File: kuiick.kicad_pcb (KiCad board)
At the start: 2 copper layers, 15 x 19 mm, 22 parts, among them J1 10118193-0001LF, J2 I2C_STANDARDQWIIC, J3 Conn_01x07, J4 Conn_01x07, SW1 SW_SPST, SW2 SW_SPST, U1 MK32L2B_QFN32, U2 W25Q32JVSS

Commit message: fully routed dip 16
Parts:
- J3, J4: value Conn_01x07 -> Conn_01x08; footprint footprint:PinHeader_1x07_P100mil_Vertical -> footprint:PinHeader_1x08_P100mil_Vertical
- moved R7 1.80 mm to (146.0, 97.8)
- moved J3 1.27 mm to (143.7, 108.9)
- moved J4 1.27 mm to (156.3, 108.9)
- moved R5 1.04 mm to (145.7, 93.0), turned to 90 degrees
- moved C1 0.82 mm to (149.8, 105.1), turned to 0 degrees
- moved J1 0.50 mm to (150.0, 108.6)
- moved J2 0.40 mm to (150.0, 94.8)
- moved U2 0.40 mm to (150.0, 93.0)
- moved R4 0.30 mm to (145.7, 95.0), turned to -90 degrees
- moved C8 0.30 mm to (154.0, 94.0)
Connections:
- J3 pad 1: /AN -> /NMI#
- J3 pad 2: /NMI# -> /RST#
- J3 pad 3: /RST# -> /SWC
- J3 pad 4: /SWC -> /SWD
- J3 pad 5: /SWD -> GND
- J3 pad 6: GND -> /3V3
- J3 pad 7: /3V3 -> /SCL
- J4 pad 1: /+5V -> /AN
- J4 pad 2: /FX7 -> /+5V
- J4 pad 3: /FX6 -> /FX7
- J4 pad 4: /FX5 -> /FX6
- J4 pad 5: /FX4 -> /FX5
- J4 pad 6: GND -> /FX4
- J4 pad 7: /3V3 -> GND
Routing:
- net GND: track 80.8 -> 66.5 mm, vias 13 -> 14
- net /AN: track 8.68 -> 17.6 mm
- net /3V3: track 61.3 -> 56.6 mm
- net /SDA: track 6.51 -> 11.0 mm
- net /RST#: track 14.9 -> 19.4 mm
- net /SCL: track 5.28 -> 8.89 mm
- net /G: track 10.4 -> 13.6 mm
- net /NMI#: track 12.2 -> 15.0 mm
- net /SWC: track 4.43 -> 5.65 mm
- net /SWD: track 5.21 -> 4.32 mm
- net /MOSI: track 16.9 -> 17.7 mm
- net /FX4: track 5.30 -> 5.92 mm
- net /FX6: track 4.45 -> 3.92 mm
- net /FX7: track 5.29 -> 4.77 mm
- net /FX5: track 4.22 -> 4.75 mm
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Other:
- board size 15 x 19 mm -> 15 x 20 mm

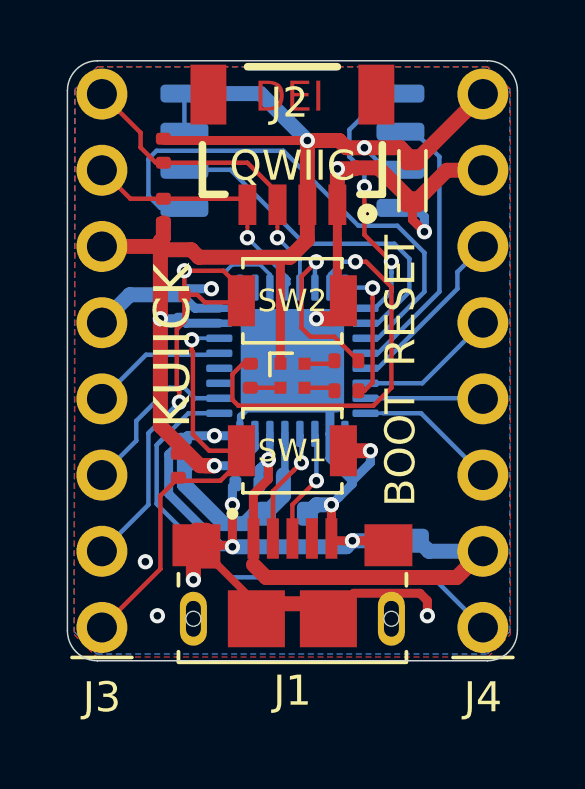
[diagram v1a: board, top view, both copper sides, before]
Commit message: cleaned up silk, added logo
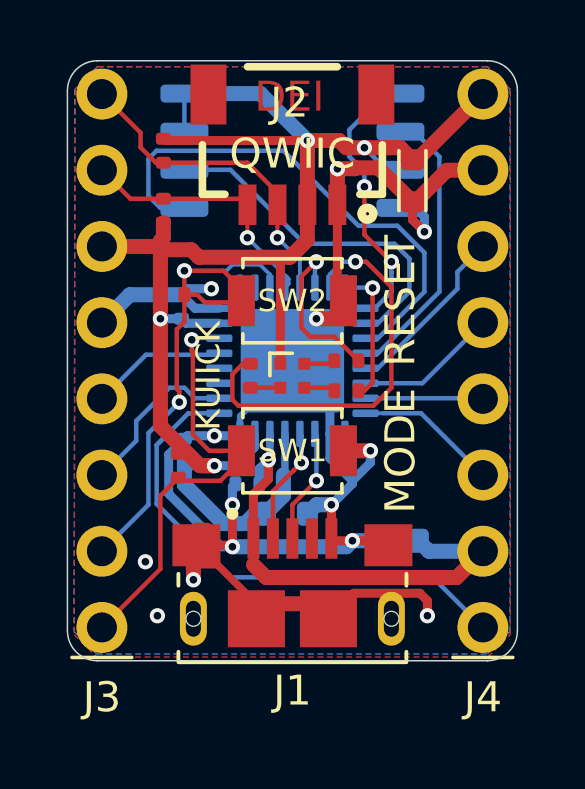
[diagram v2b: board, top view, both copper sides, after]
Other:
- board text added: "+3"
- board text added: "+5"
- board text added: "GND"
- board text added: "MODE"
- board text added: "SCL"
- board text added: "SDA"
- board text removed: "3V"
- board text removed: "5V"
- board text removed: "BOOT"
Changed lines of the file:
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@@
   (general
     (thickness 1.6)
-    (drawings 31)
+    (drawings 35)
     (tracks 356)
     (modules 22)
@@
   (layers
     (0 "F.Cu" signal)
-    (31 "B.Cu" signal)
-    (32 "B.Adhes" user)
-    (33 "F.Adhes" user)
-    (34 "B.Paste" user)
+    (31 "B.Cu" signal hide)
+    (32 "B.Adhes" user hide)
+    (33 "F.Adhes" user hide)
+    (34 "B.Paste" user hide)
     (35 "F.Paste" user)
-    (36 "B.SilkS" user)
+    (36 "B.SilkS" user hide)
     (37 "F.SilkS" user)
-    (38 "B.Mask" user)
+    (38 "B.Mask" user hide)
     (39 "F.Mask" user)
-    (40 "Dwgs.User" user)
-    (41 "Cmts.User" user)
-    (42 "Eco1.User" user)
-    (43 "Eco2.User" user)
+    (40 "Dwgs.User" user hide)
+    (41 "Cmts.User" user hide)
+    (42 "Eco1.User" user hide)
+    (43 "Eco2.User" user hide)
     (44 "Edge.Cuts" user)
-    (45 "Margin" user)
-    (46 "B.CrtYd" user)
+    (45 "Margin" user hide)
+    (46 "B.CrtYd" user hide)
     (47 "F.CrtYd" user)
-    (48 "B.Fab" user)
+    (48 "B.Fab" user hide)
     (49 "F.Fab" user)
   )
@@
       (net 1 "GND") (solder_mask_margin 0.1016))
   )
+  (gr_poly (pts (xy 153.5 103.183334) (xy 154.029167 104.241667) (xy 152.970834 104.241667) (xy 153.5 105.3) (xy 152.441667 104.241667) (xy 152.812084 103.87125) (xy 153.5 103.87125) (xy 153.5 103.765417) (xy 152.917917 103.765417) (xy 153.5 103.183334)) (layer "B.SilkS") (width 0.010583))
+  (gr_poly (pts (xy 153.5 103.183334) (xy 154.558333 104.241667) (xy 153.5 105.3) (xy 152.970834 104.241667) (xy 153.881 104.241667) (xy 153.5 104.622667) (xy 153.5 104.770833) (xy 154.029167 104.241667) (xy 153.5 103.183334)) (layer "B.Mask") (width 0.010583))
+  (gr_text "SCL" (at 145 93.8 270) (layer "B.SilkS")
+    (effects (font (size 0.75 0.75) (thickness 0.15)) (justify mirror))
+  )
+  (gr_text "SDA" (at 145 91.3 270) (layer "B.SilkS")
+    (effects (font (size 0.75 0.75) (thickness 0.15)) (justify mirror))
+  )
   (gr_text "DEI" (at 149.9 91.2) (layer "F.Cu")
     (effects (font (size 1 1) (thickness 0.15)))
   )
-  (gr_text "Steiert\nSolutions" (at 150 108.2) (layer "B.SilkS")
-    (effects (font (size 0.75 0.75) (thickness 0.15)) (justify mirror))
-  )
-  (gr_text "by" (at 151.3 105.8) (layer "B.SilkS")
-    (effects (font (size 0.75 0.75) (thickness 0.15)) (justify mirror))
-  )
-  (gr_text "KUIICK" (at 151.4 103.9) (layer "B.SilkS")
-    (effects (font (size 0.75 0.75) (thickness 0.15)) (justify mirror))
-  )
-  (gr_text "QWIIC" (at 150 93.5) (layer "F.SilkS")
+  (gr_text "Steiert\nSolutions" (at 150 108.7) (layer "B.SilkS")
+    (effects (font (size 0.75 0.75) (thickness 0.15)) (justify mirror))
+  )
+  (gr_text "by" (at 150 112) (layer "B.SilkS")
+    (effects (font (size 0.75 0.75) (thickness 0.15)) (justify mirror))
+  )
+  (gr_text "KUIICK" (at 149.9 106.5) (layer "B.SilkS")
+    (effects (font (size 0.75 0.75) (thickness 0.15)) (justify mirror))
+  )
+  (gr_text "QWIIC" (at 150 93.1) (layer "F.SilkS")
     (effects (font (size 1 1) (thickness 0.15)))
   )
-  (gr_text "KUIICK" (at 146 99.5 90) (layer "F.SilkS")
-    (effects (font (size 1.2 1.2) (thickness 0.2)))
-  )
-  (gr_text "BOOT" (at 153.6 102.9 90) (layer "F.SilkS")
+  (gr_text "KUIICK" (at 147.2 100.5 90) (layer "F.SilkS")
+    (effects (font (size 0.8 0.8) (thickness 0.2)))
+  )
+  (gr_text "MODE" (at 153.6 103 90) (layer "F.SilkS")
     (effects (font (size 1 1) (thickness 0.15)))
   )
@@
     (effects (font (size 0.75 0.75) (thickness 0.15)) (justify mirror))
   )
-  (gr_text "3V" (at 155.2 91.2) (layer "B.SilkS")
-    (effects (font (size 0.75 0.75) (thickness 0.15)) (justify mirror))
-  )
-  (gr_text "G" (at 155.2 93.9) (layer "B.SilkS")
-    (effects (font (size 0.75 0.75) (thickness 0.15)) (justify mirror))
-  )
-  (gr_text "G" (at 144.7 93.7) (layer "B.SilkS")
-    (effects (font (size 0.75 0.75) (thickness 0.15)) (justify mirror))
-  )
-  (gr_text "3V" (at 144.8 91.2) (layer "B.SilkS")
-    (effects (font (size 0.75 0.75) (thickness 0.15)) (justify mirror))
-  )
-  (gr_text "F7" (at 154.6 104.7) (layer "B.SilkS")
-    (effects (font (size 0.75 0.75) (thickness 0.15)) (justify mirror))
-  )
-  (gr_text "F6" (at 154.6 102.5) (layer "B.SilkS")
-    (effects (font (size 0.75 0.75) (thickness 0.15)) (justify mirror))
-  )
-  (gr_text "F5" (at 154.6 100.1) (layer "B.SilkS")
-    (effects (font (size 0.75 0.75) (thickness 0.15)) (justify mirror))
-  )
-  (gr_text "F4" (at 154.6 97.5) (layer "B.SilkS")
-    (effects (font (size 0.75 0.75) (thickness 0.15)) (justify mirror))
-  )
-  (gr_text "5V" (at 154.6 107.6) (layer "B.SilkS")
-    (effects (font (size 0.75 0.75) (thickness 0.15)) (justify mirror))
-  )
-  (gr_text "AN" (at 145.3 107.7) (layer "B.SilkS")
-    (effects (font (size 0.75 0.75) (thickness 0.15)) (justify mirror))
-  )
-  (gr_text "NMI" (at 145.7 105.1) (layer "B.SilkS")
-    (effects (font (size 0.75 0.75) (thickness 0.15)) (justify mirror))
-  )
-  (gr_text "RST" (at 145.6 101.8) (layer "B.SilkS")
-    (effects (font (size 0.75 0.75) (thickness 0.15)) (justify mirror))
-  )
-  (gr_text "SWC" (at 145.9 96.9) (layer "B.SilkS")
-    (effects (font (size 0.75 0.75) (thickness 0.15)) (justify mirror))
-  )
-  (gr_text "SWD" (at 145.8 100) (layer "B.SilkS")
-    (effects (font (size 0.75 0.75) (thickness 0.15)) (justify mirror))
-  )
+  (gr_text "+3" (at 155.4 92.3) (layer "B.SilkS")
+    (effects (font (size 0.75 0.75) (thickness 0.15)) (justify mirror))
+  )
+  (gr_text "G" (at 155.2 94.6) (layer "B.SilkS")
+    (effects (font (size 0.75 0.75) (thickness 0.15)) (justify mirror))
+  )
+  (gr_text "GND" (at 145.2 98.7 270) (layer "B.SilkS")
+    (effects (font (size 0.75 0.75) (thickness 0.15)) (justify mirror))
+  )
+  (gr_text "+3" (at 145.2 96.4 270) (layer "B.SilkS")
+    (effects (font (size 0.75 0.75) (thickness 0.15)) (justify mirror))
+  )
+  (gr_text "F7" (at 154.6 102.7) (layer "B.SilkS")
+    (effects (font (size 0.75 0.75) (thickness 0.15)) (justify mirror))
+  )
+  (gr_text "F6" (at 154.6 101.3) (layer "B.SilkS")
+    (effects (font (size 0.75 0.75) (thickness 0.15)) (justify mirror))
+  )
+  (gr_text "F5" (at 154.6 98.8) (layer "B.SilkS")
+    (effects (font (size 0.75 0.75) (thickness 0.15)) (justify mirror))
+  )
+  (gr_text "F4" (at 154.6 96.7) (layer "B.SilkS")
+    (effects (font (size 0.75 0.75) (thickness 0.15)) (justify mirror))
+  )
+  (gr_text "+5" (at 155.1 107.2) (layer "B.SilkS")
+    (effects (font (size 0.75 0.75) (thickness 0.15)) (justify mirror))
+  )
+  (gr_text "AN" (at 154.7 109.3) (layer "B.SilkS")
+    (effects (font (size 0.75 0.75) (thickness 0.15)) (justify mirror))
+  )
+  (gr_text "NMI" (at 145.2 108.8 270) (layer "B.SilkS")
+    (effects (font (size 0.75 0.75) (thickness 0.15)) (justify mirror))
+  )
+  (gr_text "RST" (at 145.2 106.4 270) (layer "B.SilkS")
+    (effects (font (size 0.75 0.75) (thickness 0.15)) (justify mirror))
+  )
+  (gr_text "SWC" (at 145.2 103.8 270) (layer "B.SilkS")
+    (effects (font (size 0.75 0.75) (thickness 0.15)) (justify mirror))
+  )
+  (gr_text "SWD" (at 145.2 101.3 270) (layer "B.SilkS")
+    (effects (font (size 0.75 0.75) (thickness 0.15)) (justify mirror))
+  )

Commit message: clean up silk, swapped qwiic footprint
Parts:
- J2: footprint Connectors:1X04_1MM_RA -> Connector_JST:JST_SH_SM04B-SRSS-TB_1x04-1MP_P1.00mm_Horizontal
- moved J2 2.00 mm to (150.0, 92.8)
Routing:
- net /RST#: track 19.4 -> 17.4 mm
- net /SCL: track 8.89 -> 8.31 mm
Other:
- board text added: "K32L USB to IIC Kit"
- board text removed: "by"

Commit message: clean up fills
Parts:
- moved C8 0.41 mm to (154.1, 93.6)
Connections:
- J1 pad None: (no net) -> GND
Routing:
- net GND: track 66.5 -> 75.7 mm, vias 14 -> 15
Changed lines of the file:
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@@
     (thickness 1.6)
     (drawings 37)
-    (tracks 351)
+    (tracks 357)
     (modules 22)
     (nets 33)
@@
       (dielectric_constraints no)
     )
-    (last_trace_width 0.3)
+    (last_trace_width 0.25)
     (user_trace_width 0.127)
     (user_trace_width 0.15)
@@
     (pad "S5" thru_hole oval (at -3.3 0) (size 0.9 1.8) (drill oval 0.5 1.2) (layers *.Cu *.Mask)
       (net 1 "GND"))
-    (pad "None" np_thru_hole circle (at 3.3 0) (size 0.5 0.5) (drill 0.5) (layers *.Cu *.Mask))
+    (pad "None" np_thru_hole circle (at 3.3 0) (size 0.5 0.5) (drill 0.5) (layers *.Cu *.Mask)
+      (net 1 "GND"))
     (pad "None" np_thru_hole circle (at -3.3 0) (size 0.5 0.5) (drill 0.5) (layers *.Cu *.Mask))
     (pad "S3" smd rect (at 1.2 0) (size 1.9 1.9) (layers "F.Cu" "F.Paste" "F.Mask")
@@
   )
   (module "footprint:C0603" (layer "F.Cu")
-    (at 154 94 -90)
+    (at 154.1 93.6 -90)
     (descr "Capacitor SMD 0603 (1608 Metric), square (rectangular) end terminal, IPC_7351 nominal, (Body size source: http://www.tortai-tech.com/upload/download/2011102023233369053.pdf), generated with kicad-footprint-generator")
     (tags "capacitor")
@@
   )
   (dimension 20 (width 0.1) (layer "Dwgs.User")
-    (gr_text "20.000 mm" (at 162.25 100 270) (layer "Dwgs.User")
-      (effects (font (size 1 1) (thickness 0.15)))
-    )
-    (feature1 (pts (xy 160 110) (xy 161.586421 110)))
-    (feature2 (pts (xy 160 90) (xy 161.586421 90)))
-    (crossbar (pts (xy 161 90) (xy 161 110)))
-    (arrow1a (pts (xy 161 110) (xy 160.413579 108.873496)))
-    (arrow1b (pts (xy 161 110) (xy 161.586421 108.873496)))
-    (arrow2a (pts (xy 161 90) (xy 160.413579 91.126504)))
-    (arrow2b (pts (xy 161 90) (xy 161.586421 91.126504)))
+    (gr_text "20.000 mm" (at 161.75 100 270) (layer "Dwgs.User")
+      (effects (font (size 1 1) (thickness 0.15)))
+    )
+    (feature1 (pts (xy 159.5 110) (xy 161.086421 110)))
+    (feature2 (pts (xy 159.5 90) (xy 161.086421 90)))
+    (crossbar (pts (xy 160.5 90) (xy 160.5 110)))
+    (arrow1a (pts (xy 160.5 110) (xy 159.913579 108.873496)))
+    (arrow1b (pts (xy 160.5 110) (xy 161.086421 108.873496)))
+    (arrow2a (pts (xy 160.5 90) (xy 159.913579 91.126504)))
+    (arrow2b (pts (xy 160.5 90) (xy 161.086421 91.126504)))
   )
   (gr_text "KUIICK" (at 145.3 101 90) (layer "F.SilkS")
@@
   (gr_line (start 156.5 90) (end 143.5 90) (layer "Edge.Cuts") (width 0.05))
   (gr_line (start 157.5 109) (end 157.5 91) (layer "Edge.Cuts") (width 0.05))
+  (segment (start 156.35 93.65) (end 154.1 93.65) (width 0.25) (layer "F.Cu") (net 1))
+  (segment (start 154.1 93.65) (end 152.95 93.65) (width 0.25) (layer "F.Cu") (net 1))
+  (segment (start 154.1 94.3) (end 154.1 93.65) (width 0.25) (layer "F.Cu") (net 1))
+  (segment (start 151.5 93.6) (end 152.9 93.6) (width 0.25) (layer "F.Cu") (net 1))
+  (segment (start 152.9 93.6) (end 152.95 93.65) (width 0.25) (layer "F.Cu") (net 1))
+  (segment (start 154.1 94.3) (end 154.1 95.4) (width 0.15) (layer "F.Cu") (net 1))
+  (segment (start 154.1 95.4) (end 154.4 95.7) (width 0.15) (layer "F.Cu") (net 1))
+  (segment (start 153.25 93.65) (end 153.2 93.6) (width 0.15) (layer "F.Cu") (net 1))
+  (segment (start 156.35 91.11) (end 155.46 92) (width 0.5) (layer "F.Cu") (net 9))
+  (segment (start 155.46 92) (end 155.1 92) (width 0.5) (layer "F.Cu") (net 9))
+  (segment (start 155.1 92) (end 154.2 92.9) (width 0.5) (layer "F.Cu") (net 9))
+  (segment (start 154.2 92.9) (end 154.1 92.9) (width 0.5) (layer "F.Cu") (net 9))
+  (segment (start 153.6 92.9) (end 154.1 92.9) (width 0.5) (layer "F.Cu") (net 9))
+  (via (at 148.6 99.4) (size 0.508) (drill 0.254) (layers "F.Cu" "B.Cu") (net 1))
+  (segment (start 147.6 107.7) (end 147.2 107.3) (width 0.3) (layer "B.Cu") (net 1))
+  (segment (start 147.2 107.3) (end 146.7 107.3) (width 0.3) (layer "B.Cu") (net 1))
+  (segment (start 154.2 107.7) (end 147.6 107.7) (width 0.3) (layer "B.Cu") (net 1))
+  (segment (start 154.5 108) (end 154.2 107.7) (width 0.3) (layer "B.Cu") (net 1))
+  (segment (start 154.5 108.5) (end 154.5 108) (width 0.3) (layer "B.Cu") (net 1))
   (segment (start 151.2 108.6) (end 152.049988 107.750012) (width 0.3) (layer "F.Cu") (net 1))
   (segment (start 152.049988 107.750012) (end 154.250012 107.750012) (width 0.3) (layer "F.Cu") (net 1))
@@
   (segment (start 145.524982 102.75776) (end 145.891371 102.391371) (width 0.15) (layer "B.Cu") (net 17))
   (segment (start 146.532742 101.75) (end 147.5625 101.75) (width 0.15) (layer "B.Cu") (net 17))
-  (segment (start 143.65 98.73) (end 144.58 97.8) (width 0.5) (layer "B.Cu") (net 1))
+  (segment (start 143.65 98.73) (end 144.58 97.8) (width 0.25) (layer "B.Cu") (net 1))
   (segment (start 144.58 97.8) (end 146.3 97.8) (width 0.5) (layer "B.Cu") (net 1))
   (via (at 145.1 106.7) (size 0.508) (drill 0.254) (layers "F.Cu" "B.Cu") (net 1))
@@
   (segment (start 153.6 91.095) (end 153.105 91.095) (width 0.15) (layer "B.Cu") (net 30))
   (segment (start 152.4 93.7) (end 152.4 94.2) (width 0.15) (layer "B.Cu") (net 30))
-  (segment (start 154 94.7) (end 154.1 94.7) (width 0.5) (layer "F.Cu") (net 1))
-  (segment (start 155.15 93.65) (end 156.35 93.65) (width 0.5) (layer "F.Cu") (net 1))
-  (segment (start 154.1 94.7) (end 155.15 93.65) (width 0.5) (layer "F.Cu") (net 1))
   (via (at 145.5 108.5) (size 0.508) (drill 0.254) (layers "F.Cu" "B.Cu") (net 1))
   (segment (start 152.4 92.9) (end 153.135 93.635) (width 0.15) (layer "B.Cu") (net 9))
@@
   (segment (start 152.4 92.9) (end 151.8 92.9) (width 0.5) (layer "F.Cu") (net 9))
   (segment (start 152.4 92.9) (end 153.6 92.9) (width 0.5) (layer "F.Cu") (net 9))
-  (segment (start 153.6 92.9) (end 154 93.3) (width 0.5) (layer "F.Cu") (net 9))
-  (segment (start 151.5 93.6) (end 152.069078 93.6) (width 0.5) (layer "F.Cu") (net 1))
-  (segment (start 152.069078 93.6) (end 152.098079 93.570999) (width 0.5) (layer "F.Cu") (net 1))
-  (segment (start 152.098079 93.570999) (end 152.870999 93.570999) (width 0.5) (layer "F.Cu") (net 1))
-  (segment (start 152.870999 93.570999) (end 154 94.7) (width 0.5) (layer "F.Cu") (net 1))
   (via (at 152.4 92.9) (size 0.508) (drill 0.254) (layers "F.Cu" "B.Cu") (net 9))
-  (segment (start 153.875 93.3) (end 154 93.3) (width 0.3) (layer "F.Cu") (net 9))
-  (segment (start 153.9 94.7) (end 154 94.7) (width 0.3) (layer "F.Cu") (net 1))
   (segment (start 152.4 95.8) (end 152.4 94.2) (width 0.15) (layer "F.Cu") (net 30))
   (segment (start 153.3 96.7) (end 152.4 95.8) (width 0.15) (layer "F.Cu") (net 30))
   (via (at 152.4 94.2) (size 0.508) (drill 0.254) (layers "F.Cu" "B.Cu") (net 30))
-  (segment (start 154 94.7) (end 154 95.3) (width 0.3) (layer "F.Cu") (net 1))
   (segment (start 154 95.3) (end 154.4 95.7) (width 0.3) (layer "F.Cu") (net 1))
   (segment (start 154.4 95.7) (end 154.4 95.2) (width 0.3) (layer "B.Cu") (net 1))
@@
   (segment (start 146.880912 96.54999) (end 146.630922 96.3) (width 0.5) (layer "F.Cu") (net 9))
   (segment (start 146.630922 96.3) (end 145.6 96.3) (width 0.5) (layer "F.Cu") (net 9))
-  (segment (start 154 93.3) (end 154.16 93.3) (width 0.5) (layer "F.Cu") (net 9))
-  (segment (start 154.16 93.3) (end 156.35 91.11) (width 0.5) (layer "F.Cu") (net 9))
   (segment (start 151.5 93.6) (end 151.5 94.7986) (width 0.5) (layer "F.Cu") (net 1))
   (segment (start 151.5 94.7986) (end 151.4986 94.8) (width 0.5) (layer "F.Cu") (net 1))
